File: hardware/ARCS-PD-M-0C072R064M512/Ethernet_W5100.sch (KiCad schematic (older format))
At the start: 40 parts, among them J301 RJ45_LED_Shielded, SW301 SW_Push, Y301 25MHz

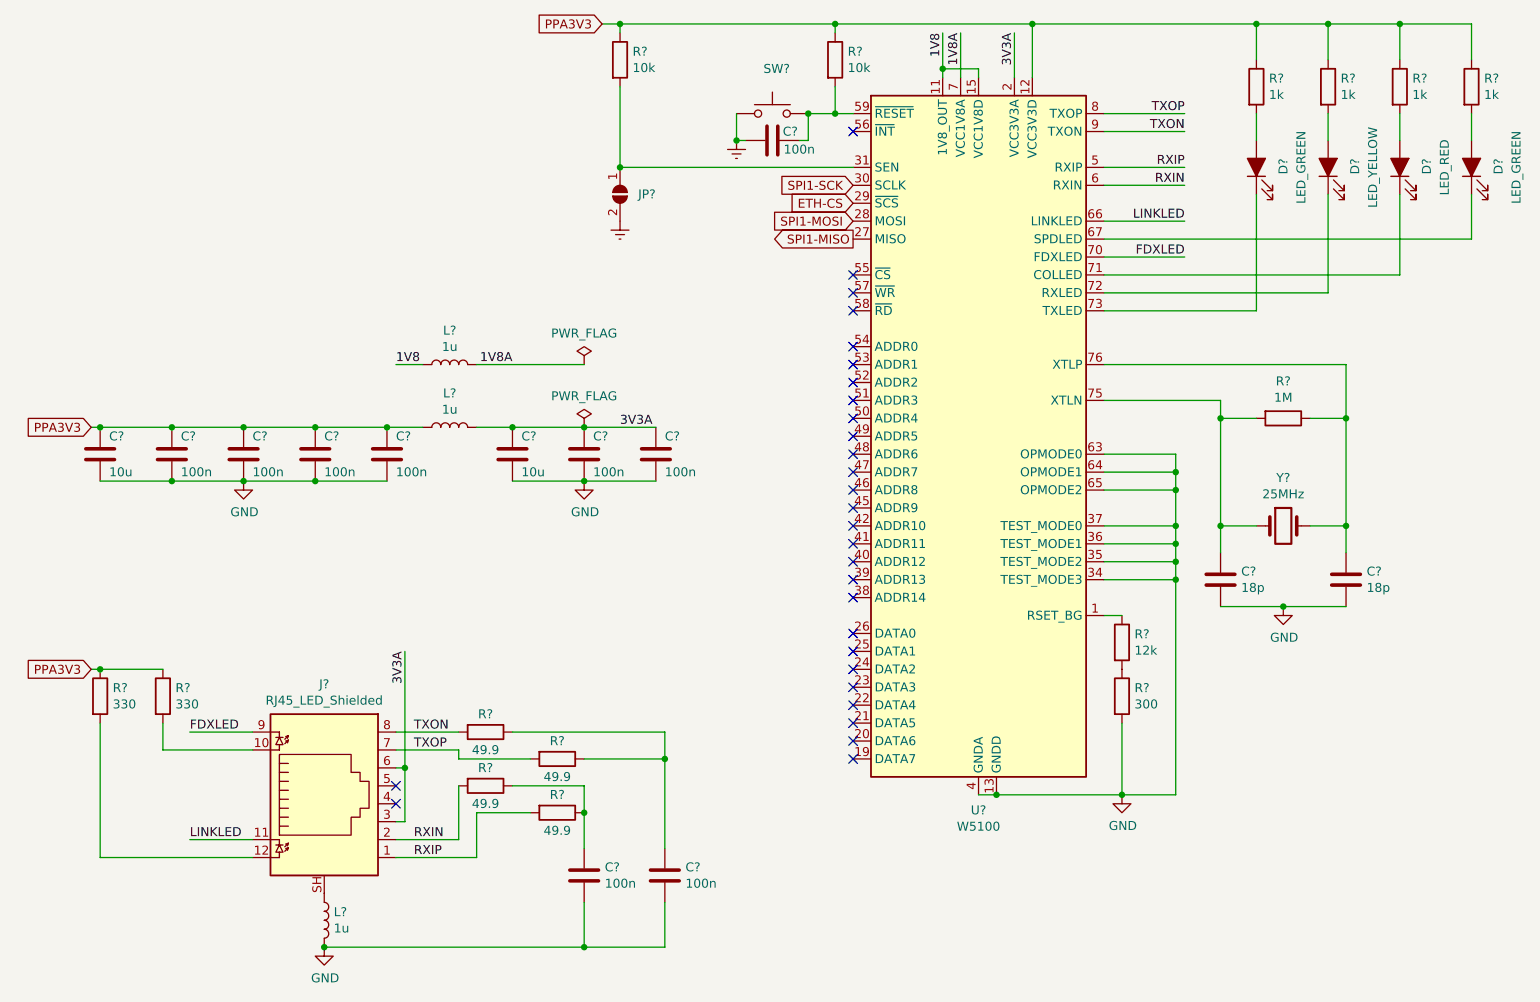
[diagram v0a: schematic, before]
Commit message: Create cards for input and output interface.
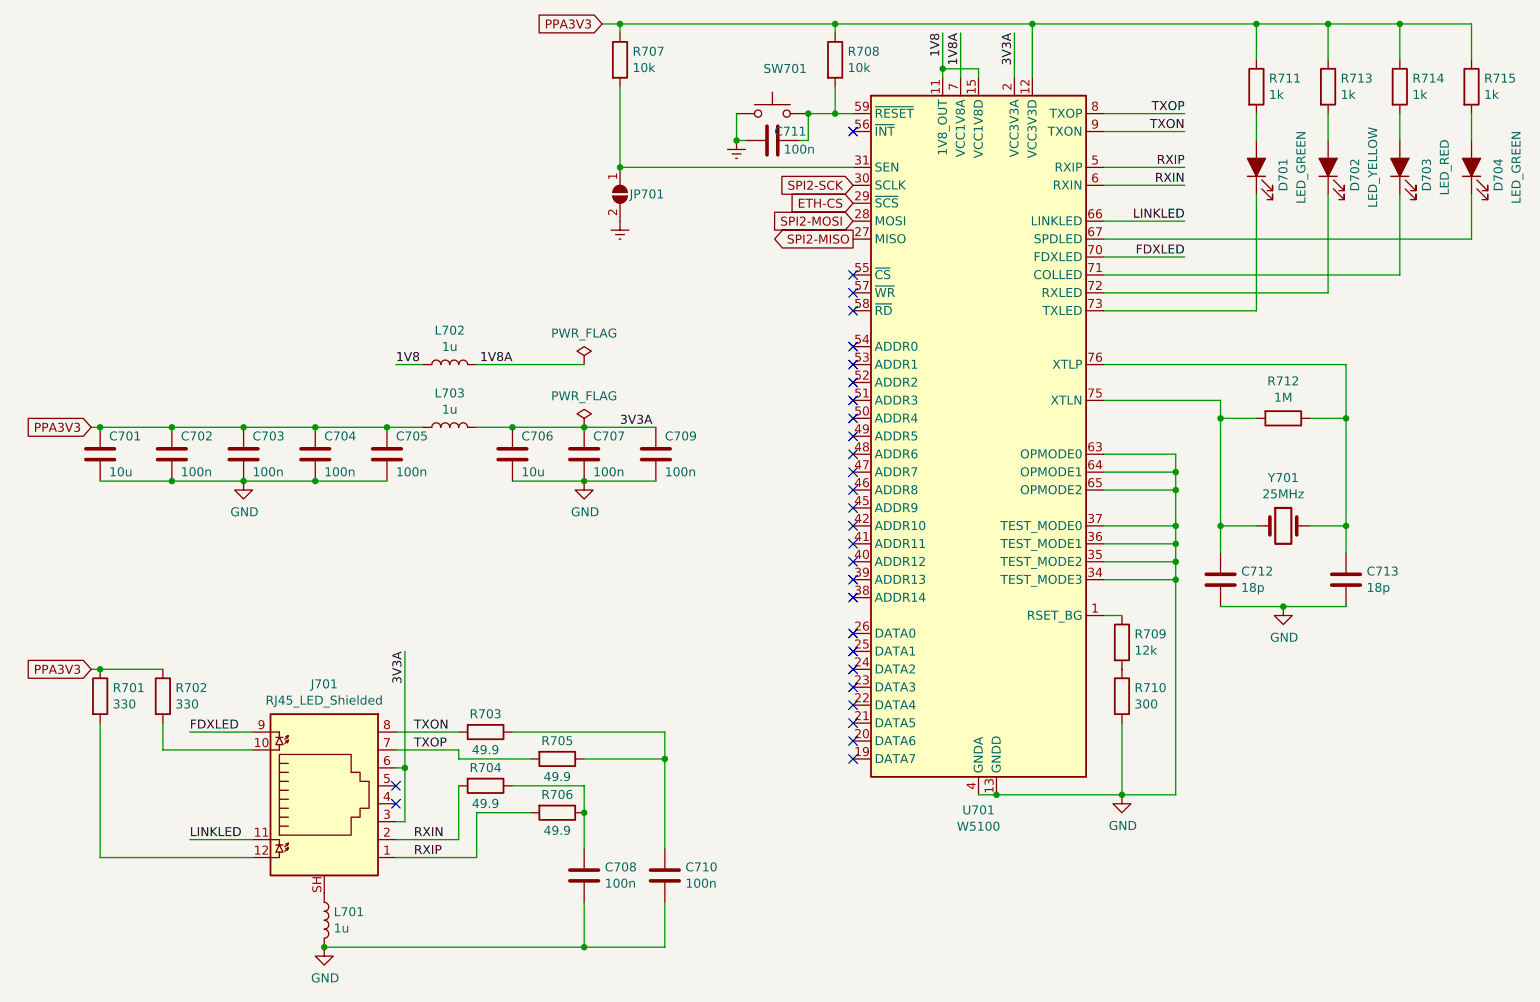
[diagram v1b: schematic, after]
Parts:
- gave numbers to parts that had none: 2
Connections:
- net SPI1-MISO renamed SPI2-MISO
- net SPI1-MOSI renamed SPI2-MOSI
- net SPI1-SCK renamed SPI2-SCK
